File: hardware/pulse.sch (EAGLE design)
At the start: 51 parts, among them IC1 MEGA8-P, IC2 MAX232, IC3 TL072P, IC4 7805TV, Q1 BF256, Q2 16MHz, T1 BC547B

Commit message: Fixed circuit and board.
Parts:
- removed C3: 100nF, rcl:C-EU025-025X050
- removed R3: 10, rcl:R-EU_0204/2V
- removed R4: 560, rcl:R-EU_0204/2V
- removed T1: BC547B, transistor:BC547-NPN-TO92-CBE
- added C21: 100nF, rcl:C-EU025-025X050
- added JP2: LED, pinhead:PINHD-1X2
- added JP8: GND, pinhead:PINHD-1X2
- added R10: 10k, rcl:R-EU_0204/7
- added R19: 500, rcl:R-EU_0204/7
- C1: device rcl:C-EU025-025X050 -> rcl:C-EU050-025X075
- C14, C17: device rcl:CPOL-EUE2.5-6 -> rcl:CPOL-EUE5-6
- C18: device rcl:C-EU025-025X050 -> rcl:C-EU102-043X133
- C20, C4: device rcl:C-EU025-025X050 -> rcl:C-EUC0805
- C9: value 10uF -> 100uF
- IC4: value 7805TV -> 7805; device linear:7805TV -> v-reg:78XXS
- JP1: device pinhead:PINHD-1X4 -> pinhead:PINHD-1X2
- JP6: device pinhead:PINHD-1X2 -> pinhead:PINHD-1X3
- JP7: device pinhead:PINHD-1X5 -> pinhead:PINHD-1X4
- L1, L2: device rcl:L-EU0204/5 -> rcl:L-EU0204/7
- Q1: value BF256 -> 2N5485; device transistor-fet:BF256 -> transistor-fet:2N5485
- R1: value 10k -> 1M
- R11, R6: device rcl:R-EU_0204/2V -> rcl:R-EU_0204/5
- R13, R14: value 470 -> 1k5
- R15, R16, R17, R18: value 470 -> 1k5; device rcl:R-EU_0204/2V -> rcl:R-EU_0207/10
- R5, R7: value 1k -> 1k5; device rcl:R-EU_0204/2V -> rcl:R-EU_0204/5
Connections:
- removed net N$5: R4.1, T1.B
- removed net N$9: Q1.G, R3.1
- new net N$11: IC1.PD6(AIN0), JP6.1
- net +5V: now also C19.1, C21.2, IC2P.VCC, IC4.OUT, R10.2; no longer IC1.AVCC, IC4.VO
- net GND: now also C1.1, C21.1, JP1.2, JP8.1, JP8.2; no longer C1.2, C3.2, JP1.4, JP7.5, T1.E
- net N$1: now also JP1.1, R2.A, R2.S; no longer JP1.3, R2.E
- net N$13: now also JP2.2; no longer JP1.2
- net N$14: now also JP2.1; no longer JP1.1
- net N$19: now also R10.1; no longer L2.2
- net N$2: now also R2.E, R6.1; no longer Q1.S, R2.A, R2.S
- net N$3: now also R19.1, R6.2; no longer R6.1
- net N$31: now also Q1.G, R1.2; no longer R4.2
- net N$34: now also JP6.3; no longer JP6.2
- net N$35: now also JP6.2; no longer JP6.1
- net N$4: now also C1.2, IC1.AVCC, L2.2; no longer R1.1, R3.2, T1.C
- net N$7: now also R19.2; no longer R6.2
- net N$8: now also IC1.PC2(ADC2); no longer IC1.PC0(ADC0)
- net VCC: now also IC4.IN; no longer C1.1, C19.1, C3.1, IC2P.VCC, IC4.VI, R1.2
- net VCC/2: now also Q1.S, R1.1
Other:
- note removed: "1) LED A 2) LED B 3) PD in 4) GND"
- moved on the sheet: C1, C10, C11, C12, C13, C14, C15, C16, C17, C18, C19, C2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

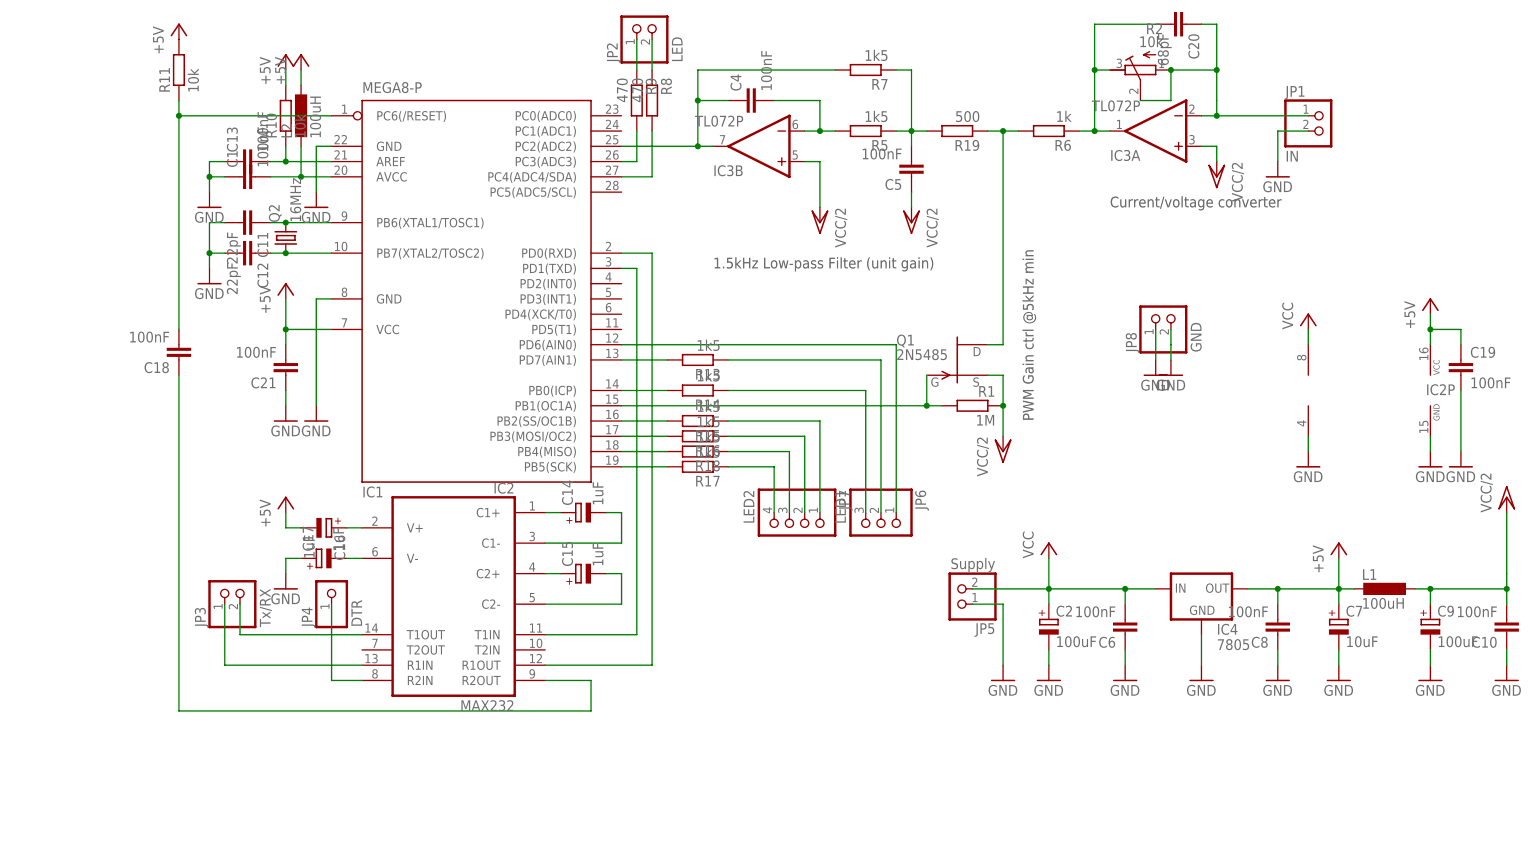
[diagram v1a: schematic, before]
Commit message: Rewritten to large parts.
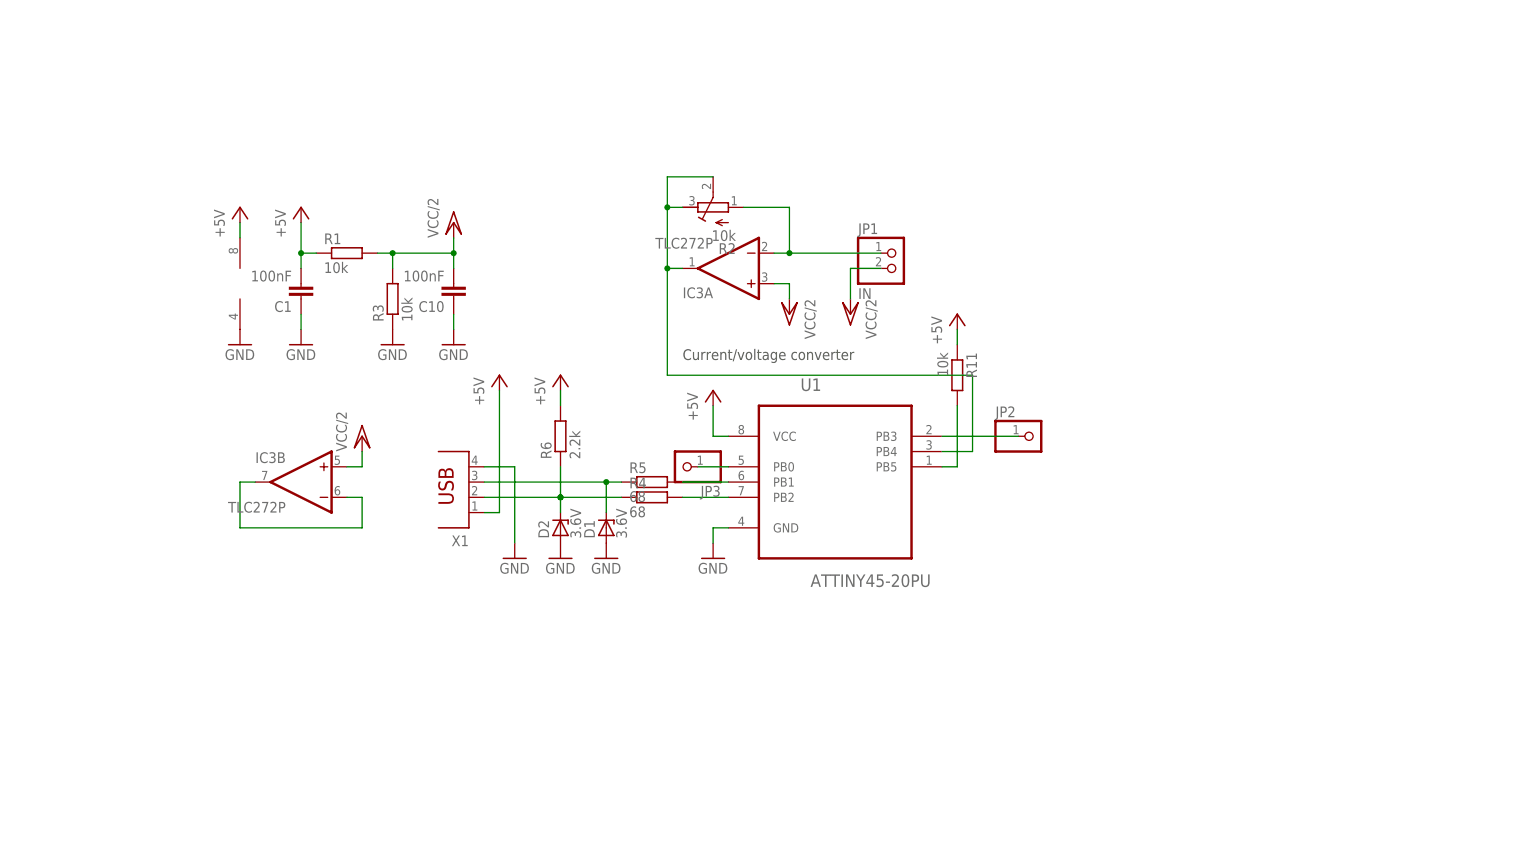
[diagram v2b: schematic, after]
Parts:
- removed C11, C12: 22pF, rcl:C-EU025-025X050
- removed C13, C19, C21, C5, C6, C8: 100nF, rcl:C-EU025-025X050
- removed C14, C17: 1uF, rcl:CPOL-EUE5-6
- removed C15, C16: 1uF, rcl:CPOL-EUE2.5-6
- removed C18: 100nF, rcl:C-EU102-043X133
- removed C2, C9: 100uF, rcl:CPOL-EUE2.5-6
- removed C20: 68pF, rcl:C-EUC0805
- removed C4: 100nF, rcl:C-EUC0805
- removed C7: 10uF, rcl:CPOL-EUE2.5-6
- removed IC1: MEGA8-P, atmel:MEGA8-P
- removed IC2: MAX232, maxim:MAX232
- removed IC4: 7805, v-reg:78XXS
- removed JP4: DTR, pinhead:PINHD-1X1
- removed JP5: Supply, pinhead:PINHD-1X2
- removed JP6: LED1, pinhead:PINHD-1X3
- removed JP7: LED2, pinhead:PINHD-1X4
- removed JP8: GND, pinhead:PINHD-1X2
- removed L1, L2: 100uH, rcl:L-EU0204/7
- removed Q1: 2N5485, transistor-fet:2N5485
- removed Q2: 16MHz, crystal:CRYSTALHC49S
- removed R10: 10k, rcl:R-EU_0204/7
- removed R13, R14: 1k5, rcl:R-EU_0204/2V
- removed R15, R16, R17, R18: 1k5, rcl:R-EU_0207/10
- removed R19: 500, rcl:R-EU_0204/7
- removed R7: 1k5, rcl:R-EU_0204/5
- removed R8, R9: 470, rcl:R-EU_0204/2V
- added D1: 3.6V, diode:ZENER-DIODEZD-2.5
- added D2: 3.6V, diode:ZENER-DIODEZD-5
- added R3: 10k, rcl:R-EU_0204/2V
- added R4: 68, rcl:R-EU_0204/2V
- added U1: ATTINY45-20PU, Atmel_By_element14_Batch_1-00:ATTINY45-20PU
- added X1: (no value), con-berg:PN87520
- C1: device rcl:C-EU050-025X075 -> rcl:C-EU075-032X103
- C10: device rcl:C-EU025-025X050 -> rcl:C-EU050-025X075
- IC3: value TL072P -> TLC272P; device linear:TL072P -> linear:TLC272P
- JP2: value LED -> (none); device pinhead:PINHD-1X2 -> pinhead:PINHD-1X1
- JP3: value Tx/RX -> (none); device pinhead:PINHD-1X2 -> pinhead:PINHD-1X1
- R1: value 1M -> 10k; device rcl:R-EU_0204/2V -> rcl:R-EU_0207/12
- R11: device rcl:R-EU_0204/5 -> rcl:R-EU_0204/7
- R5: value 1k5 -> 68; device rcl:R-EU_0204/5 -> rcl:R-EU_0204/2V
- R6: value 1k -> 2.2k; device rcl:R-EU_0204/5 -> rcl:R-EU_0204/2V
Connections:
- removed net N$13: JP2.2, R8.1
- removed net N$14: JP2.1, R9.1
- removed net N$15: C11.1, IC1.PB6(XTAL1/TOSC1), Q2.2
- removed net N$16: C12.1, IC1.PB7(XTAL2/TOSC2), Q2.1
- removed net N$17: C16.+, IC2G$1.V+
- removed net N$18: C17.-, IC2G$1.V-
- removed net N$19: C13.2, IC1.AREF, R10.1
- removed net N$2: C20.2, IC3A.OUT, R2.E, R6.1
- removed net N$20: IC2G$1.T1OUT, JP3.2
- removed net N$21: IC2G$1.R1IN, JP3.1
- removed net N$22: IC2G$1.R2IN, JP4.1
- removed net N$23: C14.-, IC2G$1.C1-
- removed net N$24: C14.+, IC2G$1.C1+
- removed net N$25: C15.+, IC2G$1.C2+
- removed net N$26: C15.-, IC2G$1.C2-
- removed net N$27: C18.2, IC1.PC6(/RESET), R11.1
- removed net N$28: C18.1, IC2G$1.R2OUT
- removed net N$29: IC1.PD1(TXD), IC2G$1.T1IN
- removed net N$30: IC1.PD0(RXD), IC2G$1.R1OUT
- removed net N$31: IC1.PB1(OC1A), Q1.G, R1.2
- removed net N$32: IC1.PC4(ADC4/SDA), R8.2
- removed net N$33: IC1.PC3(ADC3), R9.2
- removed net N$34: JP6.3, R14.1
- removed net N$35: JP6.2, R13.1
- removed net N$38: JP7.1, R15.1
- removed net N$39: JP7.2, R16.1
- removed net N$40: JP7.3, R18.1
- removed net N$41: JP7.4, R17.1
- removed net N$45: IC1.PD7(AIN1), R13.2
- removed net N$46: IC1.PB0(ICP), R14.2
- removed net N$47: IC1.PB2(SS/OC1B), R15.2
- removed net N$48: IC1.PB3(MOSI/OC2), R16.2
- removed net N$49: IC1.PB4(MISO), R18.2
- removed net N$50: IC1.PB5(SCK), R17.2
- removed net VCC: C2.+, C6.2, IC3P.V+, IC4.IN, JP5.2
- new net N$10: D1.C, R5.1, X1.3
- new net N$5: JP3.1, U1.PB0
- new net N$9: R11.2, U1.PB5
- net +5V: now also C1.2, IC3P.V+, R1.1, R11.1, R6.2, U1.VCC, X1.1; no longer C16.-, C19.1, C21.2, C7.+, C8.2, IC1.VCC@1, IC2P.VCC, IC4.OUT, L1.2, L2.1, R10.2, R11.2
- net GND: now also D1.A, D2.A, R3.1, U1.GND, X1.4; no longer C11.2, C12.2, C13.1, C17.+, C19.2, C2.-, C21.1, C6.1, C7.-, C8.1, C9.-, IC1.GND, IC1.GND@1, IC2P.GND, IC4.GND, JP1.2, JP5.1, JP8.1, JP8.2
- net N$1: no longer C20.1, R2.S
- net N$11: now also D2.C, R4.1, R6.1, X1.2; no longer IC1.PD6(AIN0), JP6.1
- net N$3: now also R4.2, U1.PB2; no longer Q1.D, R19.1, R6.2
- net N$4: now also JP2.1, U1.PB3; no longer C1.2, IC1.AVCC, L2.2
- net N$6: now also U1.PB1; no longer C4.2, IC3B.-IN
- net N$7: now also IC3B.-IN, IC3B.OUT; no longer C5.2, R19.2, R5.1, R7.1
- net N$8: now also IC3A.OUT, R2.E, R2.S, U1.PB4; no longer C4.1, IC1.PC2(ADC2), IC3B.OUT, R7.2
- net VCC/2: now also JP1.2, R1.2, R3.2; no longer C5.1, C9.+, L1.1, Q1.S, R1.1
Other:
- note removed: "1.5kHz Low-pass Filter (unit gain)"
- note removed: "PWM Gain ctrl @5kHz min"
- moved on the sheet: C1, C10, IC3A, IC3B, JP1, R1, R11, R2, R5, R6

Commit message: Fixed minors.
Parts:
- JP2: value (none) -> LED2
- JP3: value (none) -> LED1
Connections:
- removed net N$6: R5.2, U1.PB1
- new net N$2: R5.2, U1.PB2
- net N$3: now also U1.PB1; no longer U1.PB2
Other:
- moved on the sheet: IC3B, JP3
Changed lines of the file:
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@@
 <part name="C1" library="rcl" deviceset="C-EU" device="075-032X103" value="100nF"/>
 <part name="P+9" library="supply1" deviceset="VCC/2" device=""/>
-<part name="JP2" library="pinhead" deviceset="PINHD-1X1" device=""/>
-<part name="JP3" library="pinhead" deviceset="PINHD-1X1" device=""/>
+<part name="JP2" library="pinhead" deviceset="PINHD-1X1" device="" value="LED2"/>
+<part name="JP3" library="pinhead" deviceset="PINHD-1X1" device="" value="LED1"/>
 <part name="R2" library="rcl" deviceset="R-TRIMM" device="64W" value="10k"/>
 </parts>
@@
 <instances>
 <instance part="IC3" gate="A" x="93.98" y="76.2" rot="R180"/>
-<instance part="IC3" gate="B" x="22.86" y="40.64" rot="MR0"/>
+<instance part="IC3" gate="B" x="22.86" y="43.18" rot="MR0"/>
 <instance part="GND1" gate="1" x="12.7" y="63.5"/>
 <instance part="C10" gate="G$1" x="48.26" y="71.12" rot="R180"/>
@@
 <instance part="P+1" gate="G$1" x="114.3" y="68.58" rot="R180"/>
 <instance part="C1" gate="G$1" x="22.86" y="71.12" rot="R180"/>
-<instance part="P+9" gate="G$1" x="33.02" y="48.26"/>
+<instance part="P+9" gate="G$1" x="33.02" y="50.8"/>
 <instance part="JP2" gate="G$1" x="144.78" y="48.26"/>
-<instance part="JP3" gate="G$1" x="86.36" y="43.18" rot="R180"/>
+<instance part="JP3" gate="G$1" x="81.28" y="53.34" rot="R90"/>
 <instance part="R2" gate="G$1" x="91.44" y="86.36" rot="R90"/>
 </instances>
@@
 <pinref part="IC3" gate="B" pin="+IN"/>
 <pinref part="P+9" gate="G$1" pin="VCC/2"/>
-<wire x1="30.48" y1="43.18" x2="33.02" y2="43.18" width="0.1524" layer="91"/>
-<wire x1="33.02" y1="43.18" x2="33.02" y2="45.72" width="0.1524" layer="91"/>
+<wire x1="30.48" y1="45.72" x2="33.02" y2="45.72" width="0.1524" layer="91"/>
+<wire x1="33.02" y1="45.72" x2="33.02" y2="48.26" width="0.1524" layer="91"/>
 </segment>
 </net>
@@
 <segment>
 <pinref part="IC3" gate="B" pin="-IN"/>
-<wire x1="30.48" y1="38.1" x2="33.02" y2="38.1" width="0.1524" layer="91"/>
-<wire x1="33.02" y1="38.1" x2="33.02" y2="33.02" width="0.1524" layer="91"/>
+<wire x1="30.48" y1="40.64" x2="33.02" y2="40.64" width="0.1524" layer="91"/>
+<wire x1="33.02" y1="40.64" x2="33.02" y2="35.56" width="0.1524" layer="91"/>
 <pinref part="IC3" gate="B" pin="OUT"/>
-<wire x1="12.7" y1="40.64" x2="15.24" y2="40.64" width="0.1524" layer="91"/>
-<wire x1="33.02" y1="33.02" x2="12.7" y2="33.02" width="0.1524" layer="91"/>
-<wire x1="12.7" y1="33.02" x2="12.7" y2="40.64" width="0.1524" layer="91"/>
+<wire x1="12.7" y1="43.18" x2="15.24" y2="43.18" width="0.1524" layer="91"/>
+<wire x1="33.02" y1="35.56" x2="12.7" y2="35.56" width="0.1524" layer="91"/>
+<wire x1="12.7" y1="35.56" x2="12.7" y2="43.18" width="0.1524" layer="91"/>
 </segment>
 </net>
@@
 <wire x1="73.66" y1="40.64" x2="73.66" y2="35.56" width="0.1524" layer="91"/>
 <pinref part="X1" gate="G$1" pin="3"/>
+<junction x="73.66" y="40.64"/>
 <wire x1="53.34" y1="40.64" x2="73.66" y2="40.64" width="0.1524" layer="91"/>
-<junction x="73.66" y="40.64"/>
 </segment>
 </net>
@@
 <junction x="66.04" y="38.1"/>
 <junction x="66.04" y="38.1"/>
-</segment>
-</net>
-<net name="N$3" class="0">
-<segment>
-<pinref part="R4" gate="G$1" pin="2"/>
-<pinref part="U1" gate="A" pin="PB2"/>
-<wire x1="86.36" y1="38.1" x2="93.98" y2="38.1" width="0.1524" layer="91"/>
-</segment>
-</net>
-<net name="N$6" class="0">
-<segment>
-<pinref part="R5" gate="G$1" pin="2"/>
-<pinref part="U1" gate="A" pin="PB1"/>
-<wire x1="86.36" y1="40.64" x2="93.98" y2="40.64" width="0.1524" layer="91"/>
 </segment>
 </net>
@@
 <pinref part="JP3" gate="G$1" pin="1"/>
 <pinref part="U1" gate="A" pin="PB0"/>
-<wire x1="88.9" y1="43.18" x2="93.98" y2="43.18" width="0.1524" layer="91"/>
-</segment>
-</net>
+<wire x1="81.28" y1="50.8" x2="81.28" y2="43.18" width="0.1524" layer="91"/>
+<wire x1="81.28" y1="43.18" x2="93.98" y2="43.18" width="0.1524" layer="91"/>
+</segment>
+</net>
+<net name="N$2" class="0">
+<segment>
+<pinref part="U1" gate="A" pin="PB2"/>
+<wire x1="93.98" y1="38.1" x2="88.9" y2="38.1" width="0.1524" layer="91"/>
+<wire x1="88.9" y1="38.1" x2="88.9" y2="40.64" width="0.1524" layer="91"/>
+<pinref part="R5" gate="G$1" pin="2"/>
+<wire x1="88.9" y1="40.64" x2="86.36" y2="40.64" width="0.1524" layer="91"/>
+</segment>
+</net>
+<net name="N$3" class="0">
+<segment>
+<pinref part="R4" gate="G$1" pin="2"/>
+<wire x1="86.36" y1="38.1" x2="86.36" y2="35.56" width="0.1524" layer="91"/>
+<wire x1="86.36" y1="35.56" x2="91.44" y2="35.56" width="0.1524" layer="91"/>
+<wire x1="91.44" y1="35.56" x2="91.44" y2="40.64" width="0.1524" layer="91"/>
+<pinref part="U1" gate="A" pin="PB1"/>
+<wire x1="91.44" y1="40.64" x2="93.98" y2="40.64" width="0.1524" layer="91"/>
+</segment>
+</net>

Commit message: Updated schematic & board.
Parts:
- removed X1: (no value), con-berg:PN87520
- added X2: USB-A, adafruit:USB-A
- R2: value 10k -> 500k
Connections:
- net +5V: now also X2.VBUS; no longer X1.1
- net GND: now also X2.GND; no longer X1.4
- net N$10: now also X2.D+; no longer X1.3
- net N$11: now also X2.D-; no longer X1.2
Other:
- moved on the sheet: C1, C10, IC3A, IC3B, JP1, JP2, JP3, R1, R2, R3
